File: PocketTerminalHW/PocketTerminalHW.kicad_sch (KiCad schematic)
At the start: 182 parts, among them J1 USB4105-GF-A, J2 DM3D-SF, J3 53261-0271, J4 Conn_01x04, J5 Conn_01x02, J6 68712414522, J7 USB4105-GF-A, J8 66011102111302, J9 Conn_01x05, Q1 BC847BDW1, SW1 K3-1391D-5MM, U1 ESP32-S3-WROOM-1, U2 CP2102N-A02-GQFN28, U3 AMS1117-3.3 / SGM2212-3.3, U4 TP4056-42-ESOP8, U5 MT3608/SX1308, U6 CC1101RGPR, Y1 3225-26M-SR

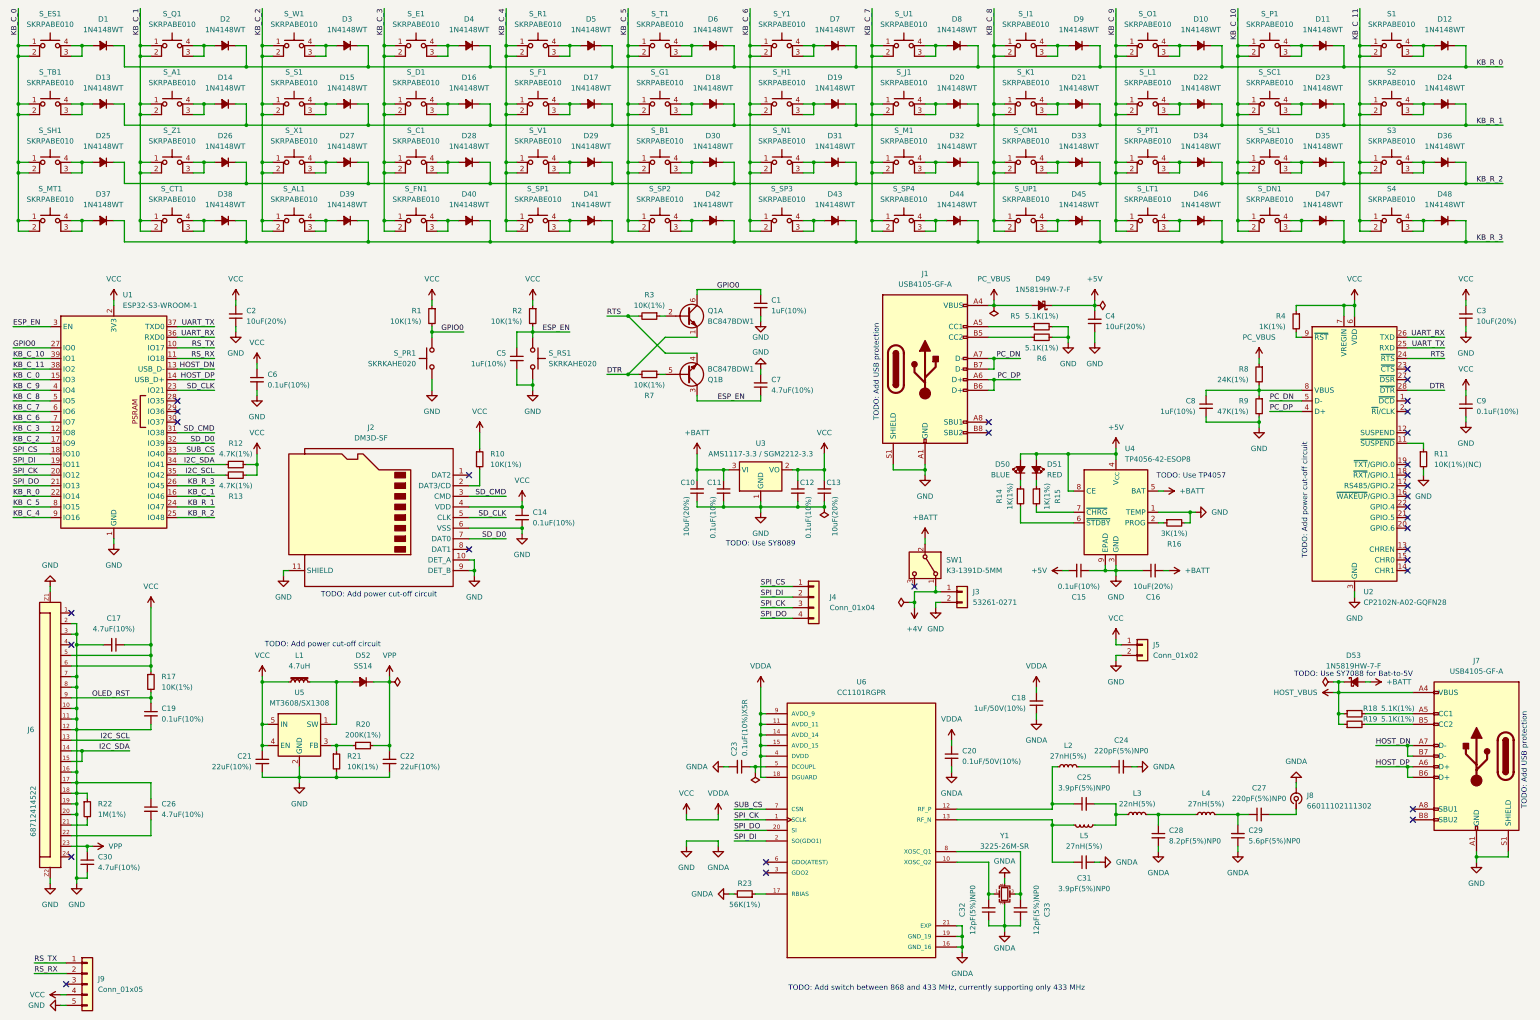
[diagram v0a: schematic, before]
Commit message: Project rename and minor PCB changes
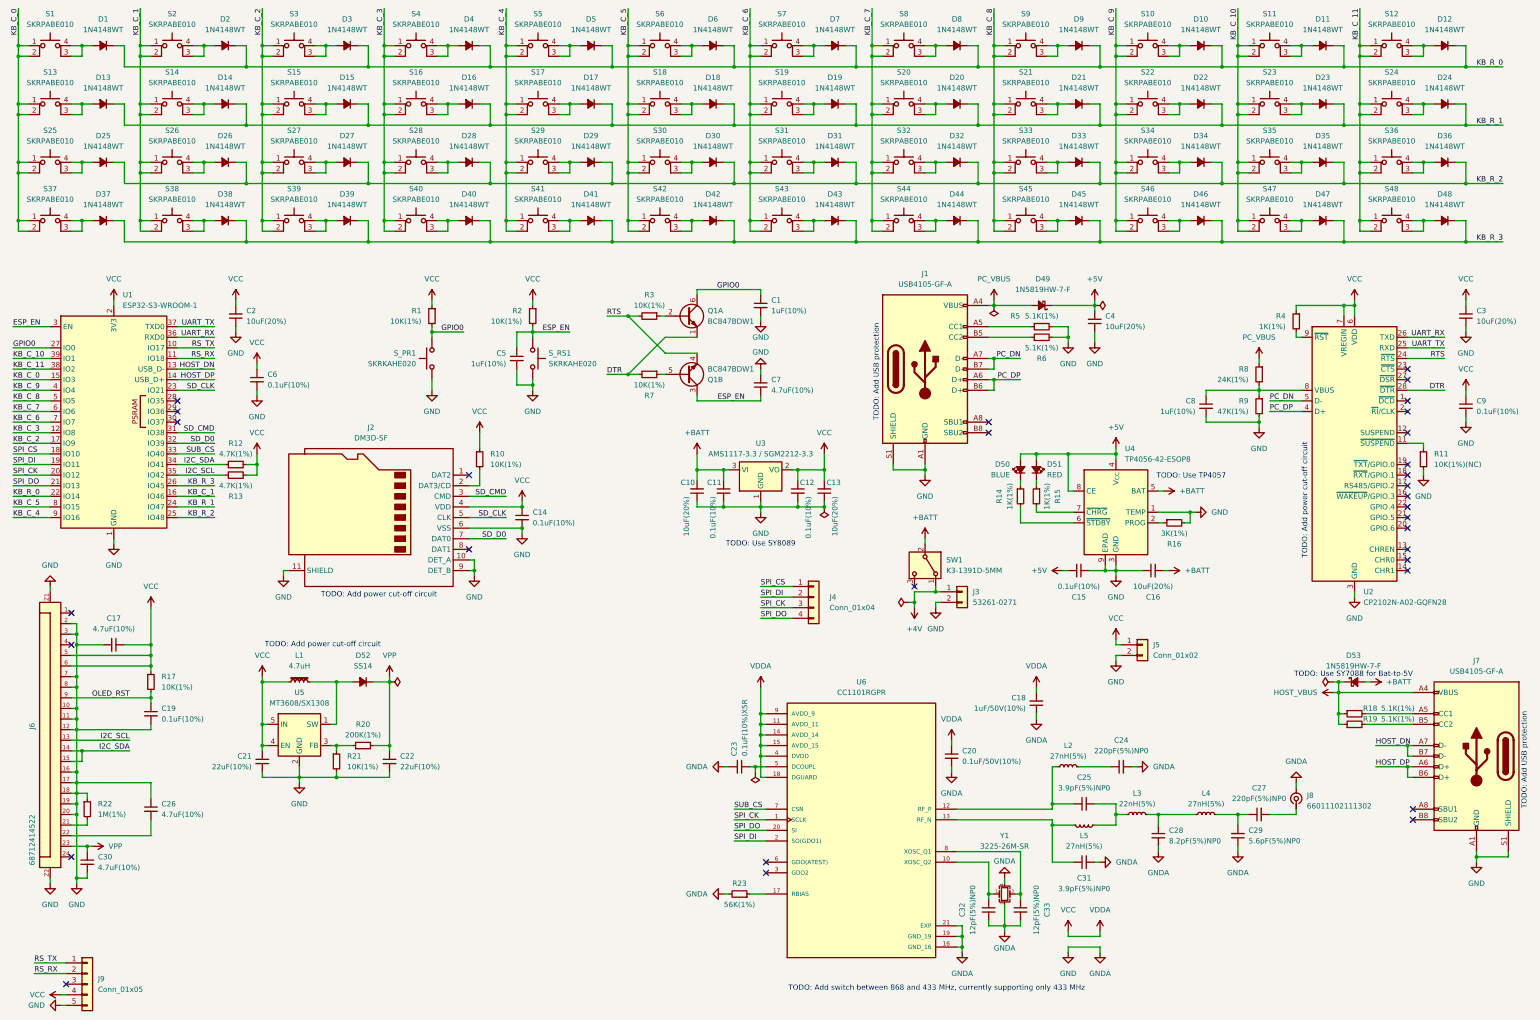
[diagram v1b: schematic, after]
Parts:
- D52: footprint Diode_SMD:D_SMA_Handsoldering -> Diode_SMD:D_SMA
- J6: footprint DataSlice:68712414522 -> PocketTerminal:68712414522; symbol DataSlice:6871XX14522_68712414522 -> PocketTerminal:6871XX14522_68712414522
- S1: renamed from S_ES1; footprint DataSlice:SW4_SKRPABE010_ALPS -> PocketTerminal:SW4_SKRPABE010_ALPS
- S10: renamed from S_O1; footprint DataSlice:SW4_SKRPABE010_ALPS -> PocketTerminal:SW4_SKRPABE010_ALPS
- S11: renamed from S_P1; footprint DataSlice:SW4_SKRPABE010_ALPS -> PocketTerminal:SW4_SKRPABE010_ALPS
- S12: renamed from S1; footprint DataSlice:SW4_SKRPABE010_ALPS -> PocketTerminal:SW4_SKRPABE010_ALPS
- S13: renamed from S_TB1; footprint DataSlice:SW4_SKRPABE010_ALPS -> PocketTerminal:SW4_SKRPABE010_ALPS
- S14: renamed from S_A1; footprint DataSlice:SW4_SKRPABE010_ALPS -> PocketTerminal:SW4_SKRPABE010_ALPS
- S15: renamed from S_S1; footprint DataSlice:SW4_SKRPABE010_ALPS -> PocketTerminal:SW4_SKRPABE010_ALPS
- S16: renamed from S_D1; footprint DataSlice:SW4_SKRPABE010_ALPS -> PocketTerminal:SW4_SKRPABE010_ALPS
- S17: renamed from S_F1; footprint DataSlice:SW4_SKRPABE010_ALPS -> PocketTerminal:SW4_SKRPABE010_ALPS
- S18: renamed from S_G1; footprint DataSlice:SW4_SKRPABE010_ALPS -> PocketTerminal:SW4_SKRPABE010_ALPS
- S19: renamed from S_H1; footprint DataSlice:SW4_SKRPABE010_ALPS -> PocketTerminal:SW4_SKRPABE010_ALPS
- S2: renamed from S_Q1; footprint DataSlice:SW4_SKRPABE010_ALPS -> PocketTerminal:SW4_SKRPABE010_ALPS
- S20: renamed from S_J1; footprint DataSlice:SW4_SKRPABE010_ALPS -> PocketTerminal:SW4_SKRPABE010_ALPS
- S21: renamed from S_K1; footprint DataSlice:SW4_SKRPABE010_ALPS -> PocketTerminal:SW4_SKRPABE010_ALPS
- S22: renamed from S_L1; footprint DataSlice:SW4_SKRPABE010_ALPS -> PocketTerminal:SW4_SKRPABE010_ALPS
- S23: renamed from S_SC1; footprint DataSlice:SW4_SKRPABE010_ALPS -> PocketTerminal:SW4_SKRPABE010_ALPS
- S24: renamed from S2; footprint DataSlice:SW4_SKRPABE010_ALPS -> PocketTerminal:SW4_SKRPABE010_ALPS
- S25: renamed from S_SH1; footprint DataSlice:SW4_SKRPABE010_ALPS -> PocketTerminal:SW4_SKRPABE010_ALPS
- S26: renamed from S_Z1; footprint DataSlice:SW4_SKRPABE010_ALPS -> PocketTerminal:SW4_SKRPABE010_ALPS
- S27: renamed from S_X1; footprint DataSlice:SW4_SKRPABE010_ALPS -> PocketTerminal:SW4_SKRPABE010_ALPS
- S28: renamed from S_C1; footprint DataSlice:SW4_SKRPABE010_ALPS -> PocketTerminal:SW4_SKRPABE010_ALPS
- S29: renamed from S_V1; footprint DataSlice:SW4_SKRPABE010_ALPS -> PocketTerminal:SW4_SKRPABE010_ALPS
- S3: renamed from S_W1; footprint DataSlice:SW4_SKRPABE010_ALPS -> PocketTerminal:SW4_SKRPABE010_ALPS
- S30: renamed from S_B1; footprint DataSlice:SW4_SKRPABE010_ALPS -> PocketTerminal:SW4_SKRPABE010_ALPS
- S31: renamed from S_N1; footprint DataSlice:SW4_SKRPABE010_ALPS -> PocketTerminal:SW4_SKRPABE010_ALPS
- S32: renamed from S_M1; footprint DataSlice:SW4_SKRPABE010_ALPS -> PocketTerminal:SW4_SKRPABE010_ALPS
- S33: renamed from S_CM1; footprint DataSlice:SW4_SKRPABE010_ALPS -> PocketTerminal:SW4_SKRPABE010_ALPS
- S34: renamed from S_PT1; footprint DataSlice:SW4_SKRPABE010_ALPS -> PocketTerminal:SW4_SKRPABE010_ALPS
- S35: renamed from S_SL1; footprint DataSlice:SW4_SKRPABE010_ALPS -> PocketTerminal:SW4_SKRPABE010_ALPS
- S36: renamed from S3; footprint DataSlice:SW4_SKRPABE010_ALPS -> PocketTerminal:SW4_SKRPABE010_ALPS
- S37: renamed from S_MT1; footprint DataSlice:SW4_SKRPABE010_ALPS -> PocketTerminal:SW4_SKRPABE010_ALPS
- S38: renamed from S_CT1; footprint DataSlice:SW4_SKRPABE010_ALPS -> PocketTerminal:SW4_SKRPABE010_ALPS
- S39: renamed from S_AL1; footprint DataSlice:SW4_SKRPABE010_ALPS -> PocketTerminal:SW4_SKRPABE010_ALPS
- S4: renamed from S_E1; footprint DataSlice:SW4_SKRPABE010_ALPS -> PocketTerminal:SW4_SKRPABE010_ALPS
- S40: renamed from S_FN1; footprint DataSlice:SW4_SKRPABE010_ALPS -> PocketTerminal:SW4_SKRPABE010_ALPS
- S41: renamed from S_SP1; footprint DataSlice:SW4_SKRPABE010_ALPS -> PocketTerminal:SW4_SKRPABE010_ALPS
- S42: renamed from S_SP2; footprint DataSlice:SW4_SKRPABE010_ALPS -> PocketTerminal:SW4_SKRPABE010_ALPS
- S43: renamed from S_SP3; footprint DataSlice:SW4_SKRPABE010_ALPS -> PocketTerminal:SW4_SKRPABE010_ALPS
- S44: renamed from S_SP4; footprint DataSlice:SW4_SKRPABE010_ALPS -> PocketTerminal:SW4_SKRPABE010_ALPS
- S45: renamed from S_UP1; footprint DataSlice:SW4_SKRPABE010_ALPS -> PocketTerminal:SW4_SKRPABE010_ALPS
- S46: renamed from S_LT1; footprint DataSlice:SW4_SKRPABE010_ALPS -> PocketTerminal:SW4_SKRPABE010_ALPS
- S47: renamed from S_DN1; footprint DataSlice:SW4_SKRPABE010_ALPS -> PocketTerminal:SW4_SKRPABE010_ALPS
- S48: renamed from S4; footprint DataSlice:SW4_SKRPABE010_ALPS -> PocketTerminal:SW4_SKRPABE010_ALPS
- S5: renamed from S_R1; footprint DataSlice:SW4_SKRPABE010_ALPS -> PocketTerminal:SW4_SKRPABE010_ALPS
- S6: renamed from S_T1; footprint DataSlice:SW4_SKRPABE010_ALPS -> PocketTerminal:SW4_SKRPABE010_ALPS
- S7: renamed from S_Y1; footprint DataSlice:SW4_SKRPABE010_ALPS -> PocketTerminal:SW4_SKRPABE010_ALPS
- S8: renamed from S_U1; footprint DataSlice:SW4_SKRPABE010_ALPS -> PocketTerminal:SW4_SKRPABE010_ALPS
- S9: renamed from S_I1; footprint DataSlice:SW4_SKRPABE010_ALPS -> PocketTerminal:SW4_SKRPABE010_ALPS
- U6: symbol DataSlice:CC1101RGPR -> PocketTerminal:CC1101RGPR
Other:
- moved on the sheet: R23

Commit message: Minor PCB adjustments, change charger to TP4057
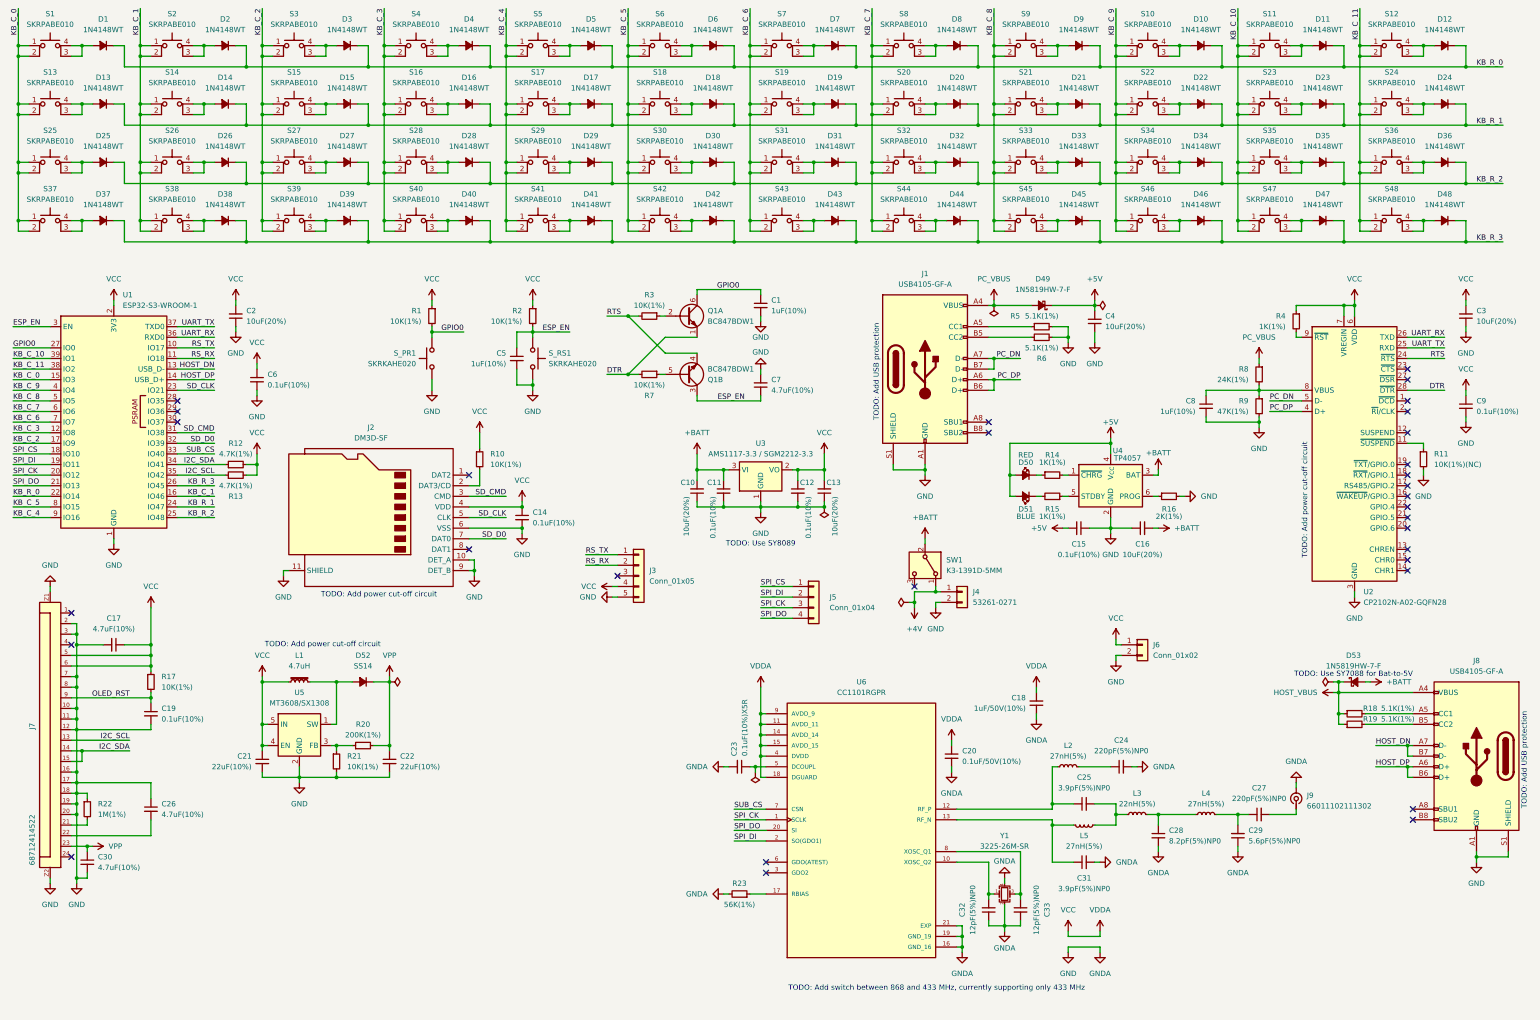
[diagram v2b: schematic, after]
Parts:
- removed U4: TP4056-42-ESOP8, Package_SO:SOIC-8-1EP_3.9x4.9mm_P1.27mm_EP2.41x3.3mm_ThermalVias, symbol Battery_Management:TP4056-42-ESOP8
- added U4: TP4057, Package_TO_SOT_SMD:TSOT-23-6, symbol Battery_Management:TP4057
- R16: value 3K(1%) -> 2K(1%)
- renumbered D51 to D50, D50 to D51, J9 to J3, J3 to J4, J4 to J5, J5 to J6, J6 to J7, J7 to J8, J8 to J9, R15 to R14, R14 to R15
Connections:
- net +5V: now also U4.4 (V_{CC})
- net +BATT: now also U4.3 (BAT)
- net GND: now also U4.2 (GND)
- net at R16.1: now also U4.6 (PROG)
- net at R15.2: now also D51.1 (K)
- net at R14.2: now also U4.1 (~{CHRG})
- net at R15.1: now also U4.5 (STDBY); no longer D51.1 (K)
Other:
- note removed: "TODO: Use TP4057"
- moved on the sheet: C15, C16, D50, D51, J3, R14, R15, R16

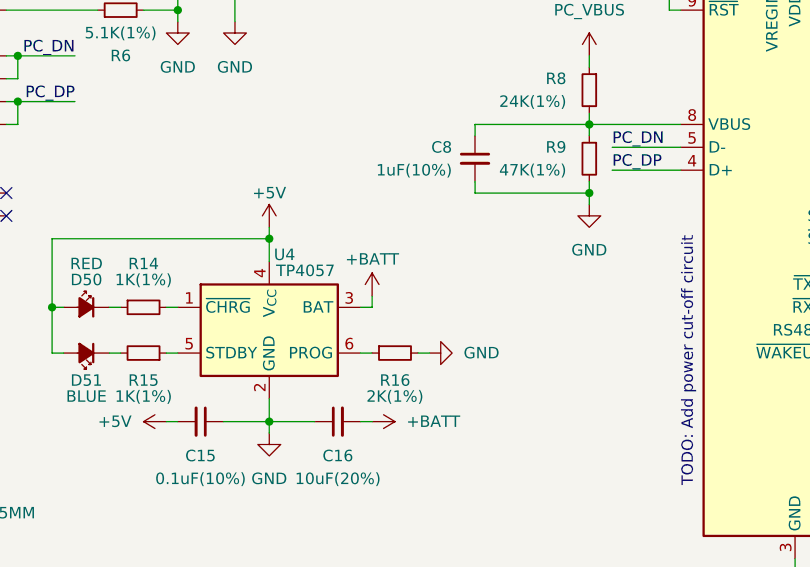
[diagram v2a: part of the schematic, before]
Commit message: Moved mounting holes
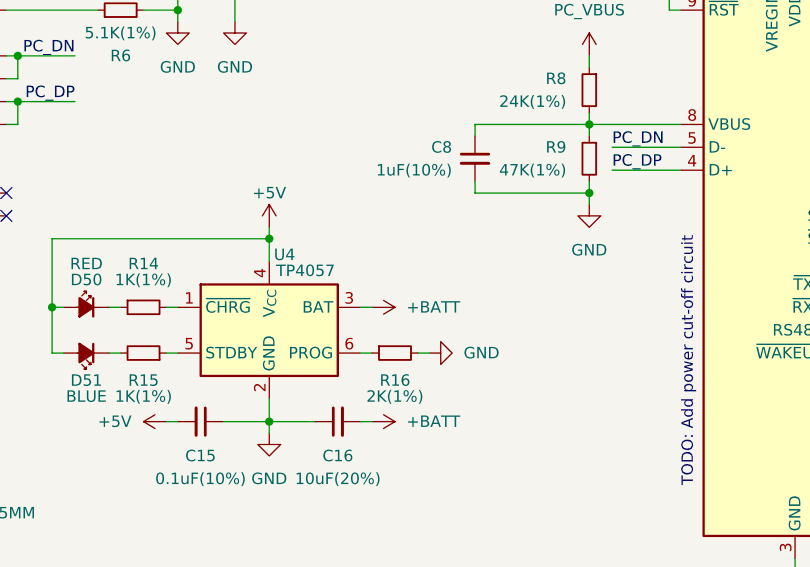
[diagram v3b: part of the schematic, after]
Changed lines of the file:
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@@
 	(wire
 		(pts
-			(xy 304.8 142.24) (xy 304.8 143.51)
-		)
-		(stroke
-			(width 0)
-			(type default)
-		)
-	)
-	(wire
-		(pts
 			(xy 279.4 227.33) (xy 279.4 236.22)
 		)
@@
 	(symbol
 		(lib_id "power:+BATT")
-		(at 304.8 142.24 0)
+		(at 304.8 143.51 270)
 		(unit 1)
 		(exclude_from_sim no)
@@
 		(on_board yes)
 		(dnp no)
-		(property "Reference" "#PWR028"
-			(at 304.8 146.05 0)
+		(fields_autoplaced yes)
+		(property "Reference" "#PWR029"
+			(at 300.99 143.51 0)
 			(effects
 				(font
@@
 		)
 		(property "Value" "+BATT"
-			(at 304.8 138.176 0)
+			(at 308.61 143.5099 90)
 			(effects
 				(font
 					(size 1.27 1.27)
 				)
+				(justify left)
 			)
 		)
 		(property "Footprint" ""
-			(at 304.8 142.24 0)
+			(at 304.8 143.51 0)
 			(effects
 				(font
@@
 		)
 		(property "Datasheet" ""
-			(at 304.8 142.24 0)
+			(at 304.8 143.51 0)
 			(effects
 				(font
@@
 		)
 		(property "Description" "Power symbol creates a global label with name \"+BATT\""
-			(at 304.8 142.24 0)
+			(at 304.8 143.51 0)
 			(effects
 				(font
@@
 			(project "DataSliceHW"
 				(path "/d4e30896-6a83-44e5-8243-667f1b9ab939"
-					(reference "#PWR028")
+					(reference "#PWR029")
 					(unit 1)
 				)
@@
 		(on_board yes)
 		(dnp no)
-		(property "Reference" "#PWR029"
+		(property "Reference" "#PWR028"
 			(at 248.92 149.86 0)
 			(effects
@@
 			(project "DataSliceHW"
 				(path "/d4e30896-6a83-44e5-8243-667f1b9ab939"
-					(reference "#PWR029")
+					(reference "#PWR028")
 					(unit 1)
 				)
